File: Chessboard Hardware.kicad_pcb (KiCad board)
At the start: 2 copper layers, 200 x 200 mm, 85 parts, among them IC1 SS49E, IC10 SS49E, IC11 SS49E, IC12 SS49E, IC13 SS49E, IC14 SS49E, IC15 SS49E, IC16 SS49E, IC17 SS49E, IC18 SS49E, IC19 SS49E, IC2 SS49E, IC20 SS49E, IC21 SS49E, IC22 SS49E, IC23 SS49E, IC24 SS49E, IC25 SS49E, IC26 SS49E, IC27 SS49E, IC28 SS49E, IC29 SS49E, IC3 SS49E, IC30 SS49E, IC31 SS49E, IC32 SS49E, IC33 SS49E, IC34 SS49E, IC35 SS49E, IC36 SS49E, IC37 SS49E, IC38 SS49E, IC39 SS49E, IC4 SS49E, IC40 SS49E, IC41 SS49E, IC42 SS49E, IC43 SS49E, IC44 SS49E, IC45 SS49E, IC46 SS49E, IC47 SS49E, IC48 SS49E, IC49 SS49E, IC5 SS49E, IC50 SS49E, IC51 SS49E, IC52 SS49E, IC53 SS49E, IC54 SS49E, IC55 SS49E, IC56 SS49E, IC57 SS49E, IC58 SS49E, IC59 SS49E, IC6 SS49E, IC60 SS49E, IC61 SS49E, IC62 SS49E, IC63 SS49E, IC64 SS49E, IC65 CD74HC4067M96, IC66 CD74HC4067M96, IC67 CD74HC4067M96, IC68 CD74HC4067M96, IC7 SS49E, IC8 SS49E, IC9 SS49E, J1 Conn_01x04_Pin

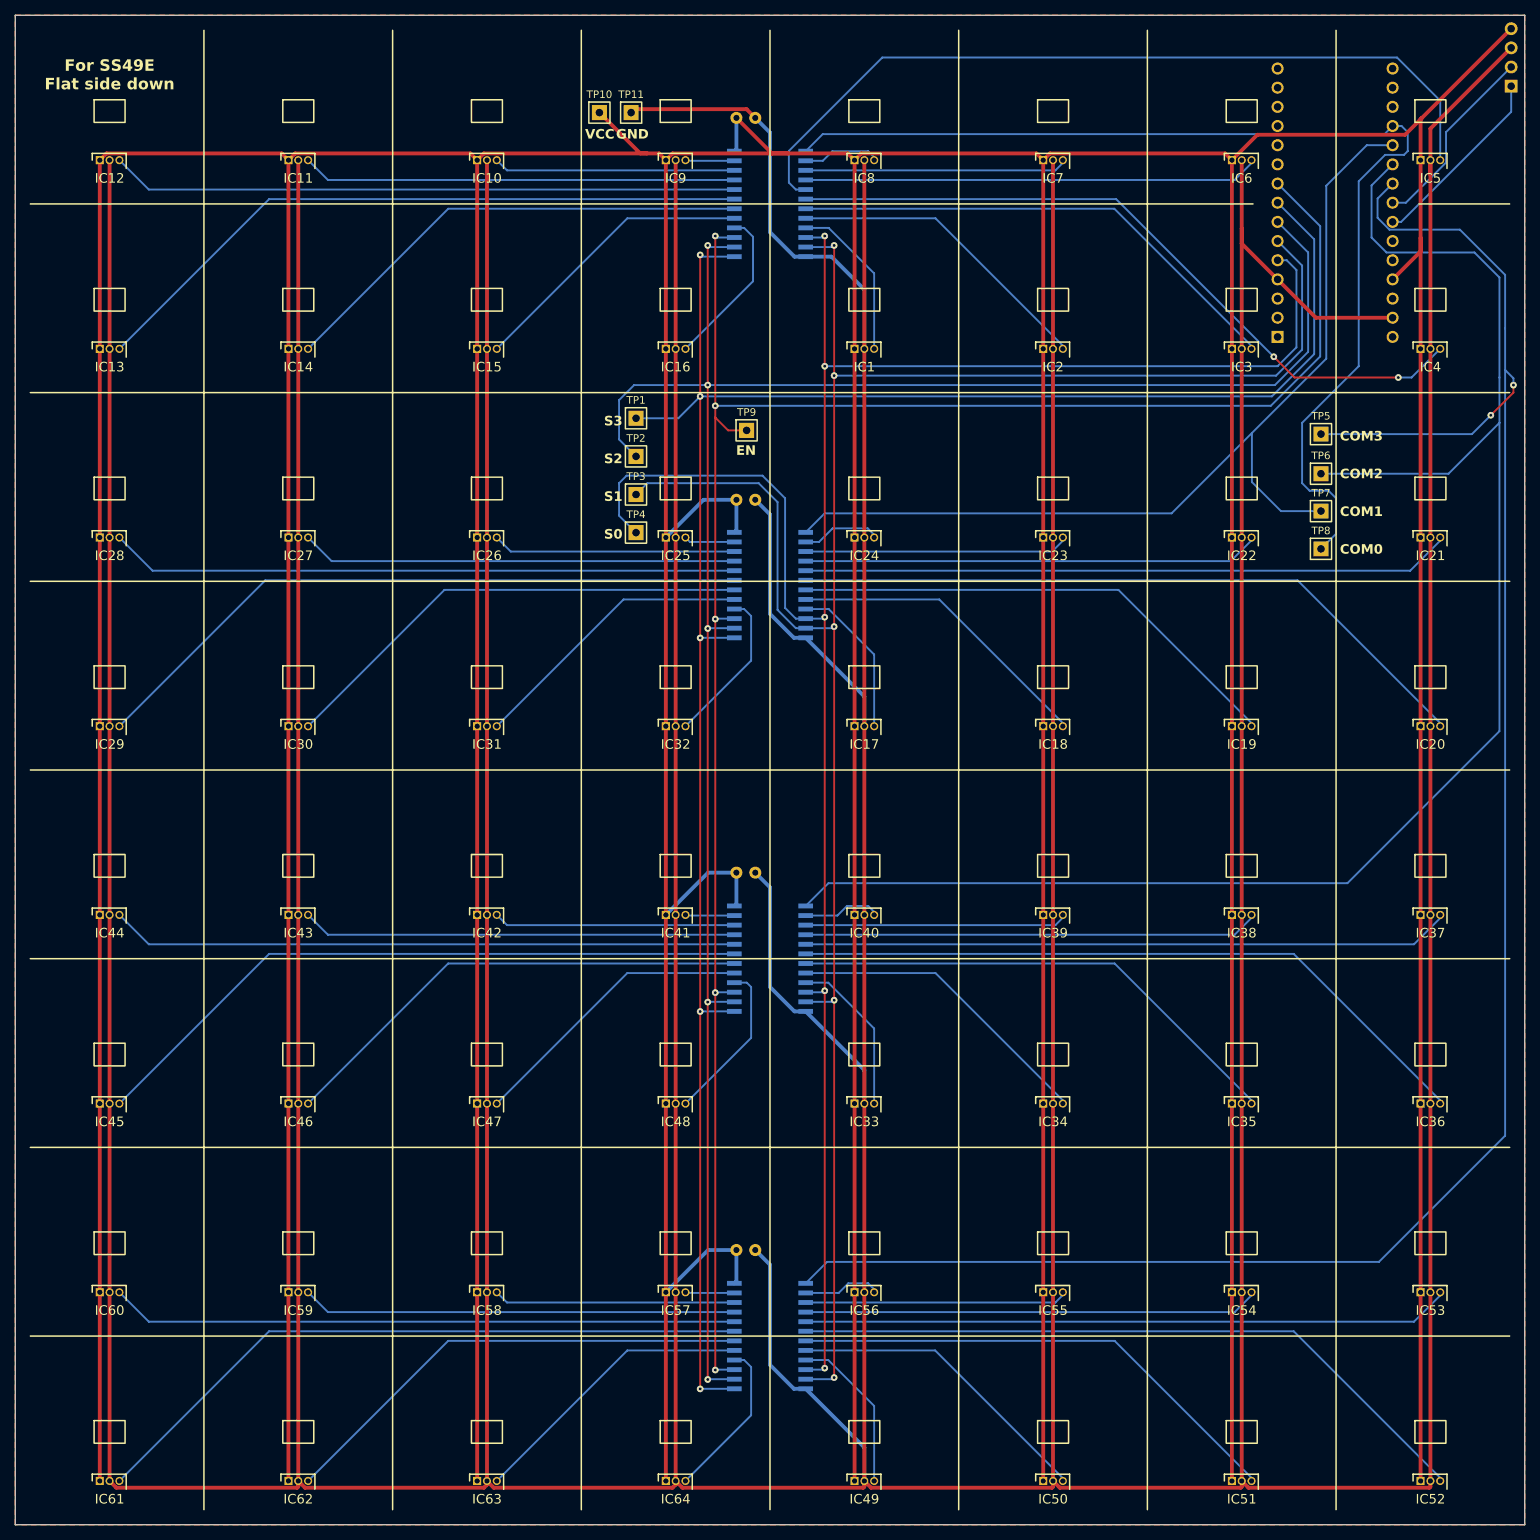
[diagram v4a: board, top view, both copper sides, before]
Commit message: Add 4 pin header to all sides for convenience
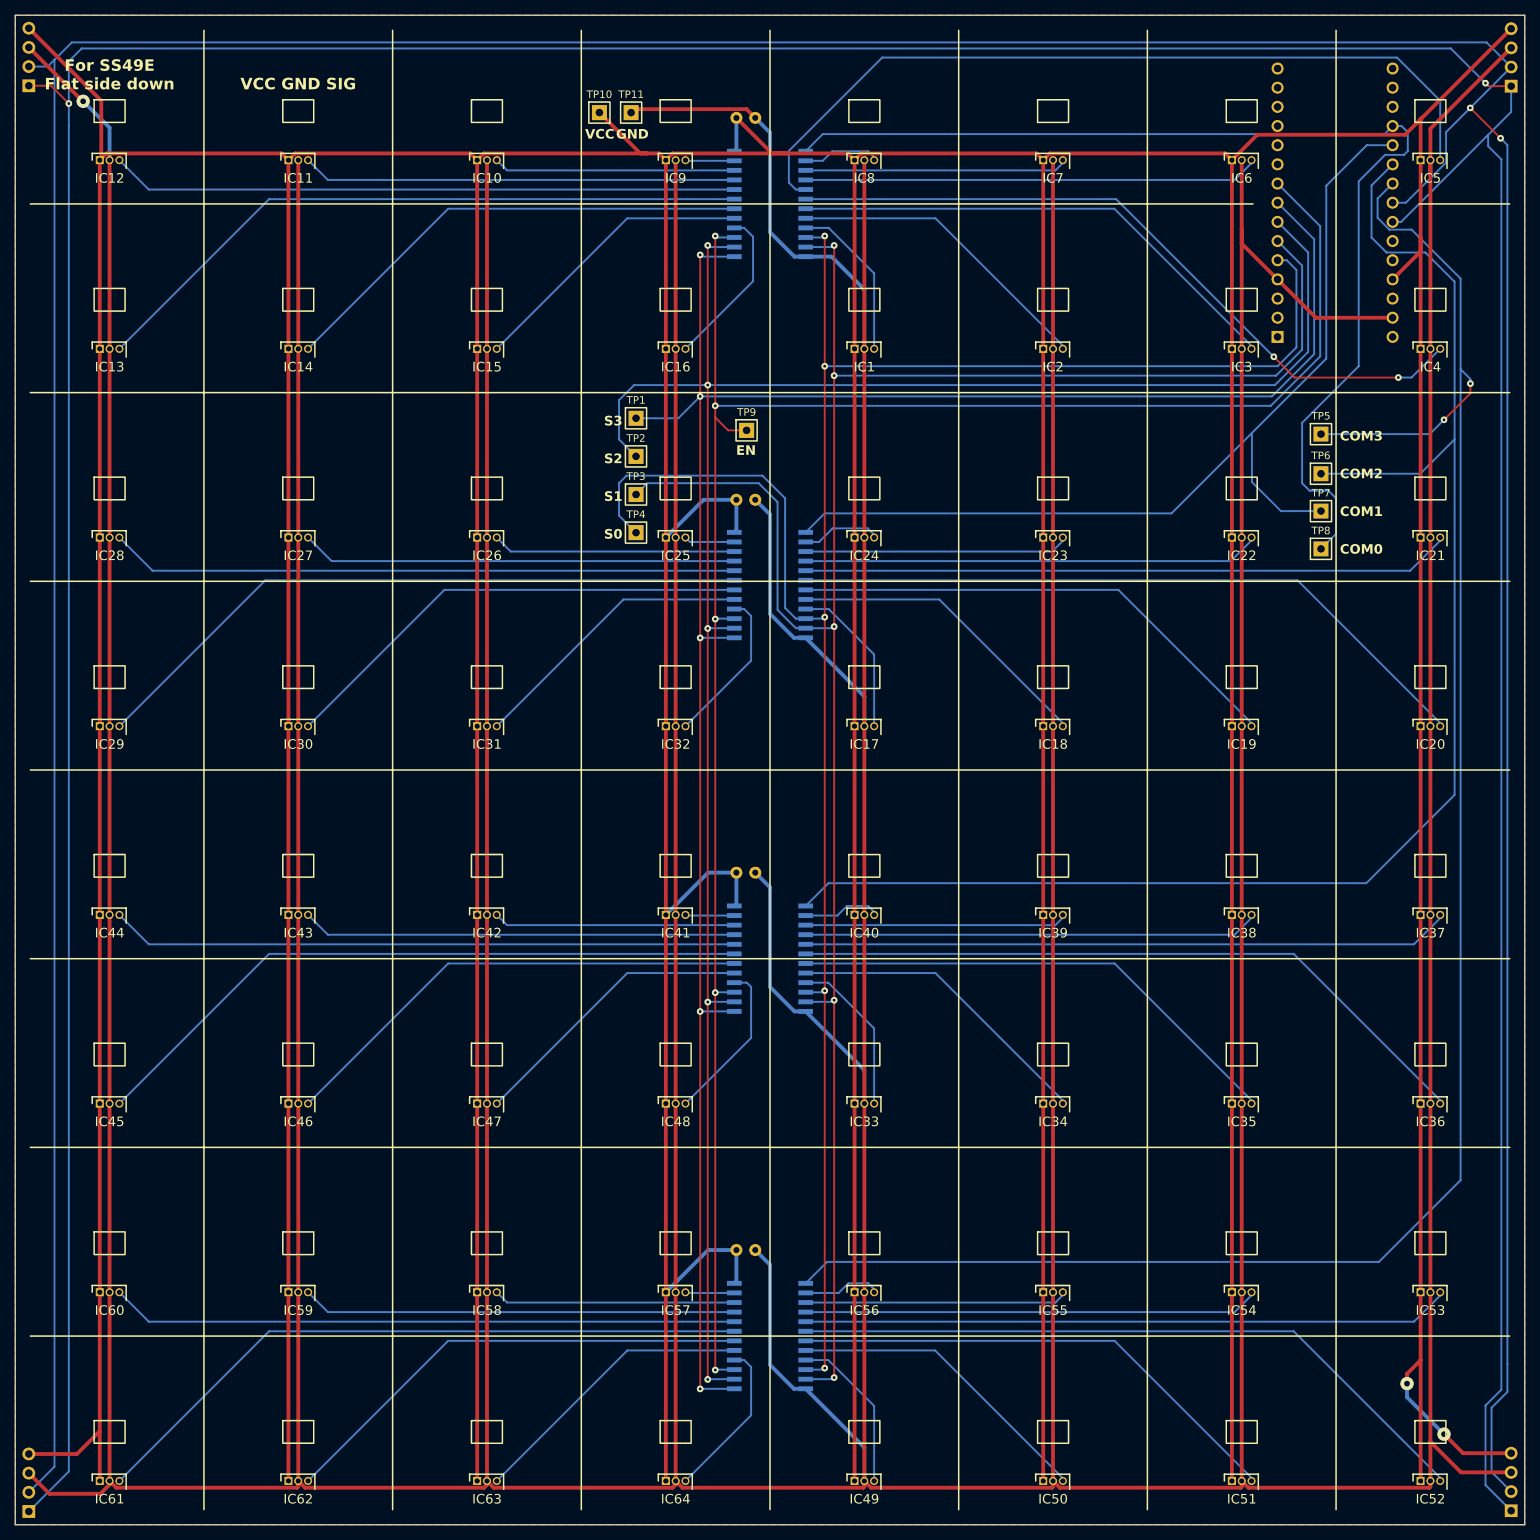
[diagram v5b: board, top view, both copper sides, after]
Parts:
- added J2: Conn_01x04_Pin, Connector_PinHeader_2.54mm:PinHeader_1x04_P2.54mm_Vertical, B.Cu at (51.8, 59.3)
- added J3: Conn_01x04_Pin, Connector_PinHeader_2.54mm:PinHeader_1x04_P2.54mm_Vertical, B.Cu at (51.8, 248.2)
- added J4: Conn_01x04_Pin, Connector_PinHeader_2.54mm:PinHeader_1x04_P2.54mm_Vertical, B.Cu at (248.2, 248.1)
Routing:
- net /SCL: track 25.1 -> 604.9 mm, vias 0 -> 2
- net /SDA: track 25.5 -> 603.1 mm, vias 0 -> 2
- net VCC: track 1681.5 -> 1736.2 mm, vias 0 -> 2
- net GND: track 1798.7 -> 1843.3 mm, vias 0 -> 1
- net /COM2: track 218.0 -> 203.9 mm
- net /COM3: track 271.5 -> 257.4 mm
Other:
- board text added: "!!! 5V DEVICE !!!"
- board text added: "VCC GND SIG"

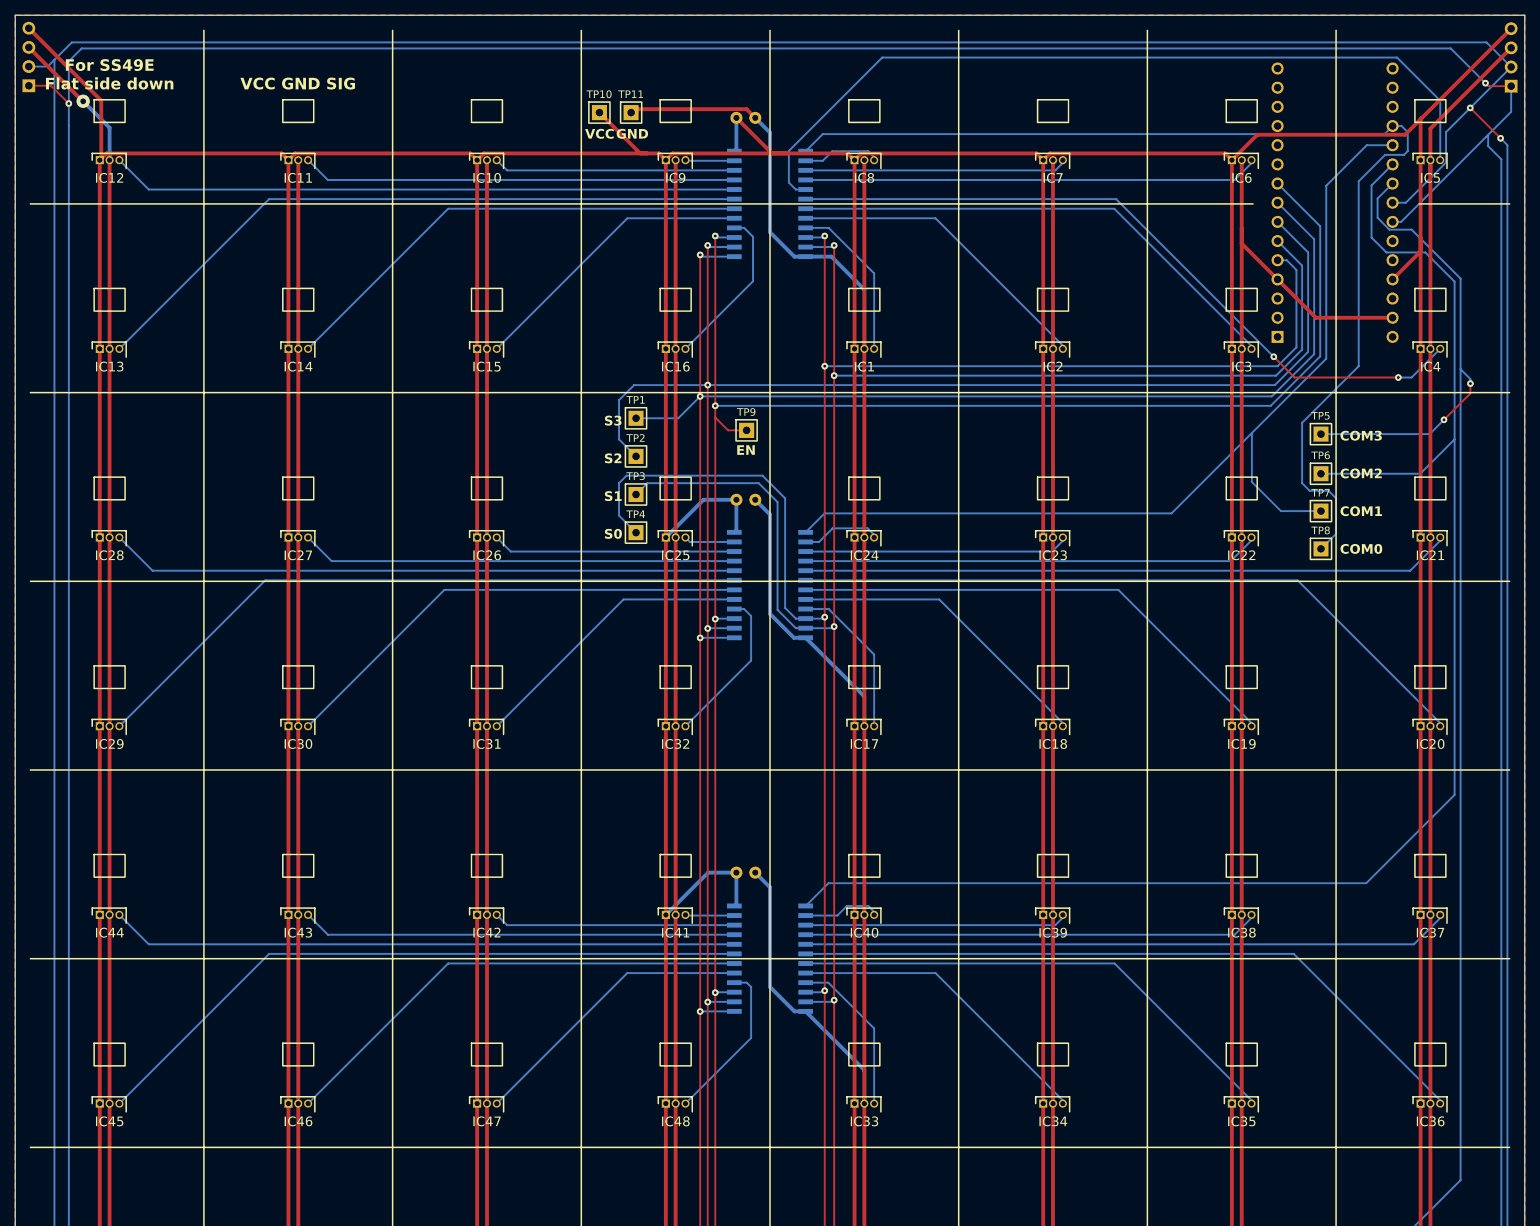
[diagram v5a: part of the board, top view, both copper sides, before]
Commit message: I2C pull ups
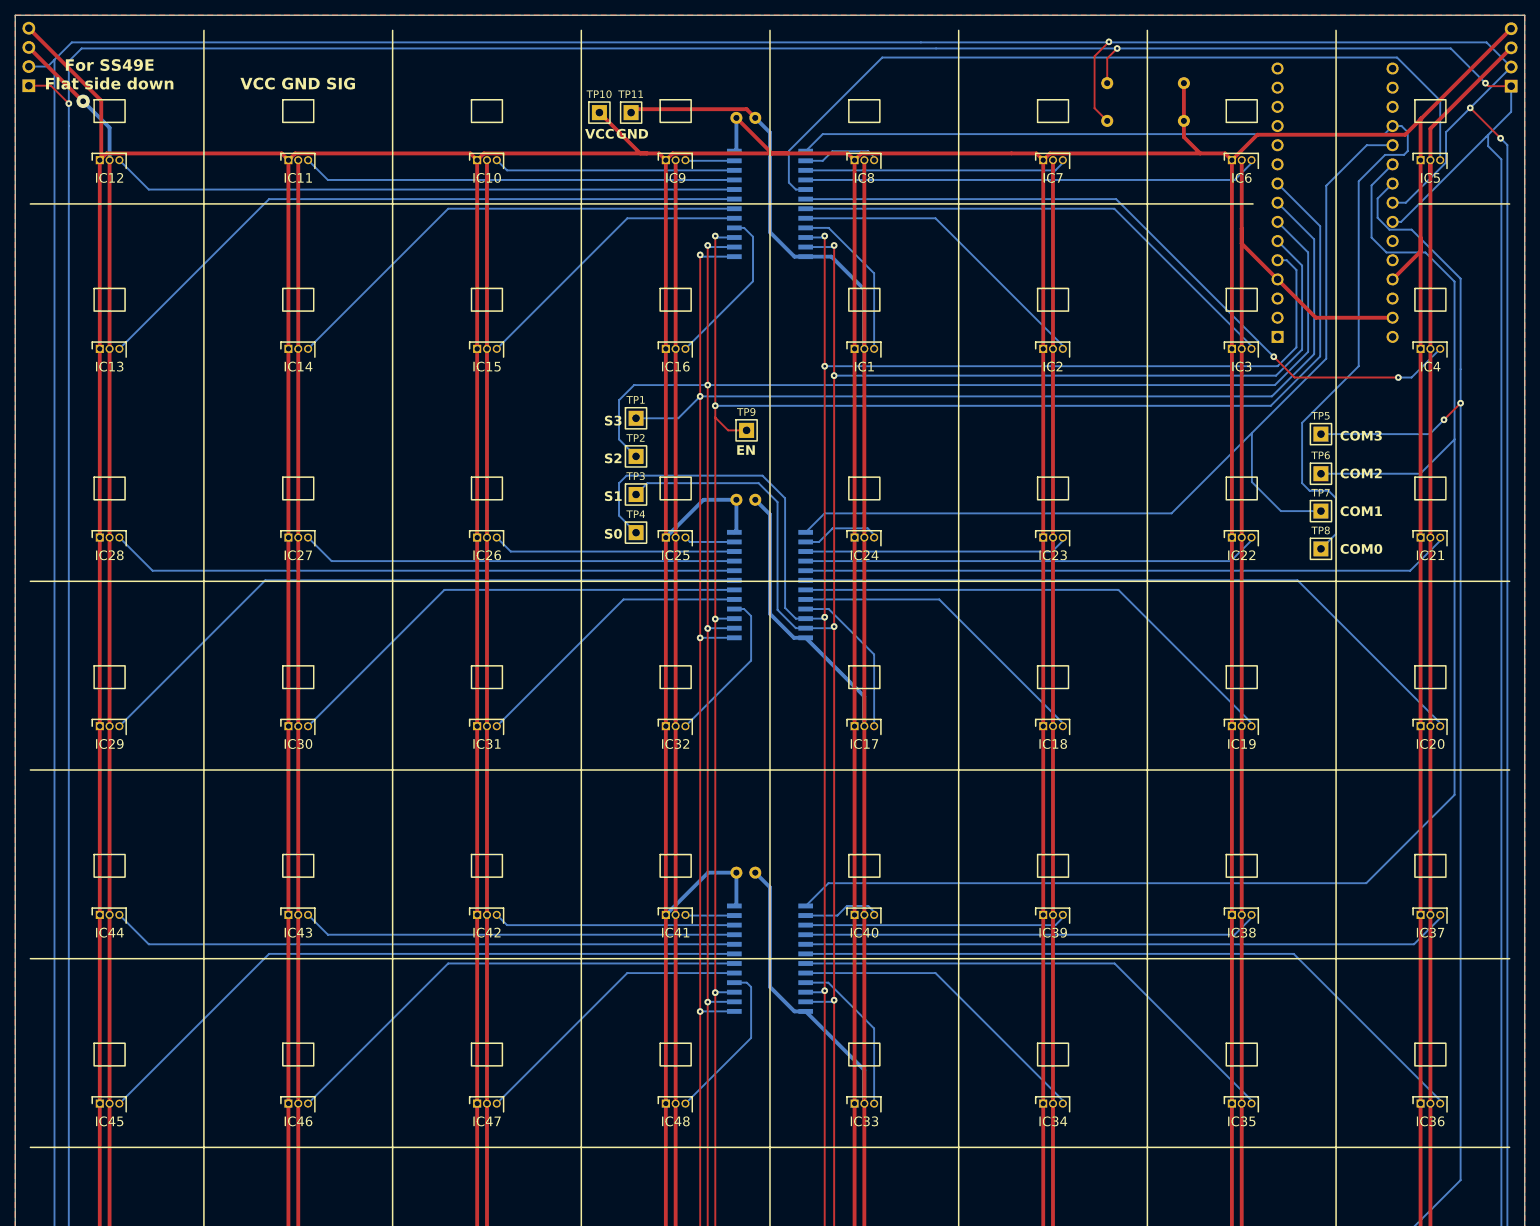
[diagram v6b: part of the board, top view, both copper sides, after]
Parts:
- added R1: 10k, Resistor_THT:R_Axial_DIN0207_L6.3mm_D2.5mm_P10.16mm_Horizontal, B.Cu at (204.8, 59.0)
- added R2: 10k, Resistor_THT:R_Axial_DIN0207_L6.3mm_D2.5mm_P10.16mm_Horizontal, B.Cu at (204.8, 64.0)
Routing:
- net /SDA: track 603.1 -> 615.1 mm, vias 2 -> 3
- net VCC: track 1736.2 -> 1746.4 mm
- net /COM3: track 257.4 -> 251.8 mm
- net /SCL: track 604.9 -> 610.1 mm, vias 2 -> 3
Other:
- board text added: "For CD74HC4067M96 Dot in top left 100nF decoupling"
- board text added: "I2C pull ups Both 10k to 5v"
- board text removed: "!!! 5V DEVICE !!!"
- board text removed: "For CD74HC4067M96 Dot in top left"

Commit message: Cleanup
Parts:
- removed J2, J3, J4: Conn_01x04_Pin, Connector_PinHeader_2.54mm:PinHeader_1x04_P2.54mm_Vertical
- moved R1 53.3 mm to (245.0, 94.1), turned to 90 degrees
- moved R2 43.3 mm to (245.0, 80.1), turned to 90 degrees
- moved TP1 0.60 mm to (132.2, 104.0)
- moved TP2 0.55 mm to (132.2, 109.0)
- moved TP3 0.50 mm to (132.2, 114.0)
- moved TP4 0.45 mm to (132.2, 119.0)
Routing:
- net /SDA: track 615.1 -> 33.4 mm, vias 3 -> 1
- net /SCL: track 610.1 -> 39.2 mm, vias 3 -> 0
- net GND: track 1843.3 -> 1795.3 mm, vias 1 -> 0
- net VCC: track 1746.4 -> 1701.3 mm
- net /S2: track 285.7 -> 286.3 mm
- net /S1: track 284.0 -> 284.5 mm

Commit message: Done
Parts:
- added H1: MountingHole, MountingHole:MountingHole_2.7mm_M2.5, F.Cu at (54.0, 54.0)
- added H2: MountingHole, MountingHole:MountingHole_2.7mm_M2.5, F.Cu at (54.0, 246.0)
- added H3: MountingHole, MountingHole:MountingHole_2.7mm_M2.5, F.Cu at (246.0, 246.0)
- added H4: MountingHole, MountingHole:MountingHole_2.7mm_M2.5, F.Cu at (246.0, 54.0)
- moved R1 9.00 mm to (245.0, 103.1)
- moved J1 8.50 mm to (248.2, 67.9)
- moved R2 8.00 mm to (245.0, 88.1)
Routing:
- net VCC: track 1701.3 -> 1729.4 mm, vias 2 -> 1
- net /SDA: track 33.4 -> 27.2 mm
- net GND: track 1795.3 -> 1791.7 mm
- net /SCL: track 39.2 -> 37.8 mm
